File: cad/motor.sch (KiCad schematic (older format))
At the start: 12 parts, among them P2 CONN_2, P3 CONN_2, P4 CONN_2, Q1 SiA910EDJ, U5 DRV8837

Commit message: everything has a footprint
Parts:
- P2, P3, P4: footprint (none) -> Pin_Headers:Pin_Header_Straight_1x02
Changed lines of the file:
@@
 F 0 "P2" H 4400 2750 50  0000 C CNN
 F 1 "CONN_2" V 4500 2600 50  0000 C CNN
-F 2 "" H 4400 2600 60  0001 C CNN
+F 2 "Pin_Headers:Pin_Header_Straight_1x02" H 4400 2600 60  0001 C CNN
 F 3 "" H 4400 2600 60  0000 C CNN
 	1    4400 2600
@@
 F 0 "P3" H 7150 2750 50  0000 C CNN
 F 1 "CONN_2" V 7250 2600 50  0000 C CNN
-F 2 "" H 7150 2600 60  0001 C CNN
+F 2 "Pin_Headers:Pin_Header_Straight_1x02" H 7150 2600 60  0001 C CNN
 F 3 "" H 7150 2600 60  0000 C CNN
 	1    7150 2600
@@
 F 0 "P4" H 7500 5100 50  0000 C CNN
 F 1 "CONN_2" V 7600 4950 50  0000 C CNN
-F 2 "" H 7500 4950 60  0001 C CNN
+F 2 "Pin_Headers:Pin_Header_Straight_1x02" H 7500 4950 60  0001 C CNN
 F 3 "" H 7500 4950 60  0000 C CNN
 	1    7500 4950

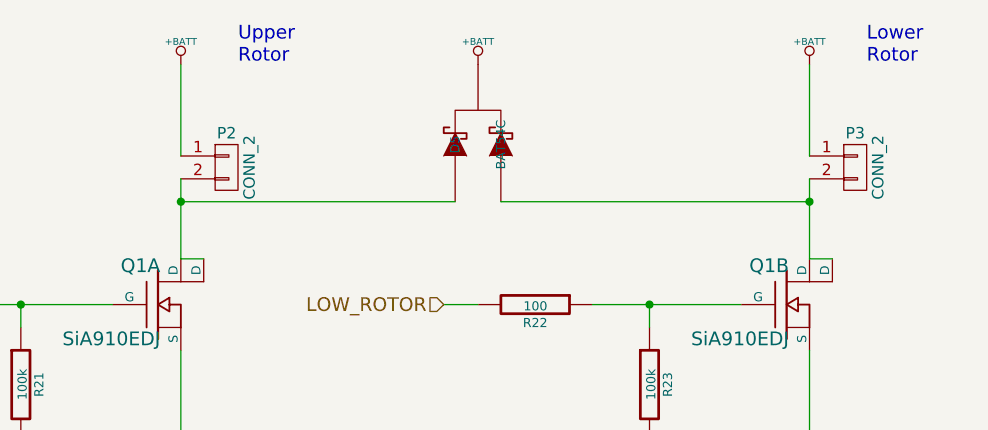
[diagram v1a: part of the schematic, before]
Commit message: made motor pads single to save space
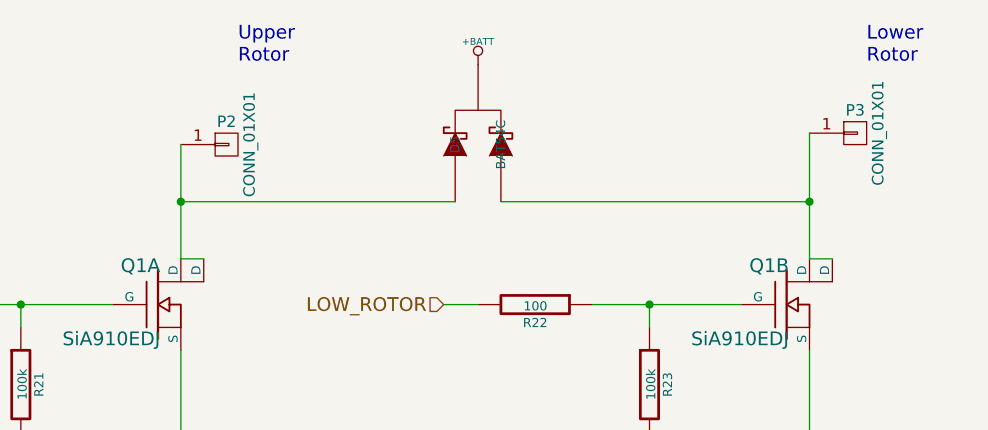
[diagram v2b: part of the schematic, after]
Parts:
- removed P2, P3: CONN_2, Pin_Headers:Pin_Header_Straight_1x02, symbol CONN_01X02
- added P2, P3: CONN_01X01, Pin_Headers:Pin_Header_Straight_1x01, symbol CONN_01X01
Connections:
- net at D5.1, Q1.6 (D), Q1.D1 (D): now also P2.1 (P1)
- net at D5.2, Q1.3 (D), Q1.D2 (D): now also P3.1 (P1)
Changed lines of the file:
@@
 Comment4 ""
 $EndDescr
-$Comp
-L CONN_01X02 P2
-U 1 1 54913051
-P 4400 2600
-F 0 "P2" H 4400 2750 50  0000 C CNN
-F 1 "CONN_2" V 4500 2600 50  0000 C CNN
-F 2 "Pin_Headers:Pin_Header_Straight_1x02" H 4400 2600 60  0001 C CNN
-F 3 "" H 4400 2600 60  0000 C CNN
-	1    4400 2600
-	1    0    0    -1
-$EndComp
-Wire Wire Line
-	4200 2650 4200 3000
-$Comp
-L +BATT #PWR070
-U 1 1 549132CE
-P 4200 2150
-F 0 "#PWR070" H 4200 2100 20  0001 C CNN
-F 1 "+BATT" H 4200 2250 30  0000 C CNN
-F 2 "" H 4200 2150 60  0000 C CNN
-F 3 "" H 4200 2150 60  0000 C CNN
-	1    4200 2150
-	1    0    0    -1
-$EndComp
-Wire Wire Line
-	4200 2150 4200 2550
+Wire Wire Line
+	4200 2500 4200 3000
 Connection ~ 4200 2750
 $Comp
@@
 	2600 3200 2750 3200
 $Comp
-L GND #PWR071
+L GND #PWR070
 U 1 1 54913D81
 P 4200 3900
-F 0 "#PWR071" H 4200 3900 30  0001 C CNN
+F 0 "#PWR070" H 4200 3900 30  0001 C CNN
 F 1 "GND" H 4200 3830 30  0001 C CNN
 F 2 "" H 4200 3900 60  0000 C CNN
@@
 $EndComp
 Connection ~ 4200 3800
-$Comp
-L CONN_01X02 P3
-U 1 1 54914313
-P 7150 2600
-F 0 "P3" H 7150 2750 50  0000 C CNN
-F 1 "CONN_2" V 7250 2600 50  0000 C CNN
-F 2 "Pin_Headers:Pin_Header_Straight_1x02" H 7150 2600 60  0001 C CNN
-F 3 "" H 7150 2600 60  0000 C CNN
-	1    7150 2600
-	1    0    0    -1
-$EndComp
-Wire Wire Line
-	6950 2650 6950 3000
-$Comp
-L +BATT #PWR072
-U 1 1 54914320
-P 6950 2150
-F 0 "#PWR072" H 6950 2100 20  0001 C CNN
-F 1 "+BATT" H 6950 2250 30  0000 C CNN
-F 2 "" H 6950 2150 60  0000 C CNN
-F 3 "" H 6950 2150 60  0000 C CNN
-	1    6950 2150
-	1    0    0    -1
-$EndComp
-Wire Wire Line
-	6950 2150 6950 2550
+Wire Wire Line
+	6950 2450 6950 3000
 Connection ~ 6950 2750
 $Comp
@@
 	5350 3200 5500 3200
 $Comp
-L GND #PWR073
+L GND #PWR071
 U 1 1 5491433E
 P 6950 3900
-F 0 "#PWR073" H 6950 3900 30  0001 C CNN
+F 0 "#PWR071" H 6950 3900 30  0001 C CNN
 F 1 "GND" H 6950 3830 30  0001 C CNN
 F 2 "" H 6950 3900 60  0000 C CNN
@@
 $EndComp
 $Comp
-L VCC #PWR074
+L VCC #PWR072
 U 1 1 5491AD60
 P 5550 5300
-F 0 "#PWR074" H 5550 5400 30  0001 C CNN
+F 0 "#PWR072" H 5550 5400 30  0001 C CNN
 F 1 "VCC" H 5550 5400 30  0000 C CNN
 F 2 "" H 5550 5300 60  0000 C CNN
@@
 $EndComp
 $Comp
-L DGND #PWR075
+L DGND #PWR073
 U 1 1 5491B7C8
 P 5550 5850
-F 0 "#PWR075" H 5550 5850 40  0001 C CNN
+F 0 "#PWR073" H 5550 5850 40  0001 C CNN
 F 1 "DGND" H 5550 5780 40  0000 C CNN
 F 2 "" H 5550 5850 60  0000 C CNN
@@
 Connection ~ 5550 5350
 $Comp
-L +BATT #PWR076
+L +BATT #PWR074
 U 1 1 5491B876
 P 5950 5550
-F 0 "#PWR076" H 5950 5500 20  0001 C CNN
+F 0 "#PWR074" H 5950 5500 20  0001 C CNN
 F 1 "+BATT" H 5950 5650 30  0000 C CNN
 F 2 "" H 5950 5550 60  0000 C CNN
@@
 $EndComp
 $Comp
-L GND #PWR077
+L GND #PWR075
 U 1 1 5491BB74
 P 5950 6100
-F 0 "#PWR077" H 5950 6100 30  0001 C CNN
+F 0 "#PWR075" H 5950 6100 30  0001 C CNN
 F 1 "GND" H 5950 6030 30  0001 C CNN
 F 2 "" H 5950 6100 60  0000 C CNN
@@
 	6100 5100 6200 5100
 $Comp
-L GND #PWR078
+L GND #PWR076
 U 1 1 5491EB14
 P 7250 5600
-F 0 "#PWR078" H 7250 5600 30  0001 C CNN
+F 0 "#PWR076" H 7250 5600 30  0001 C CNN
 F 1 "GND" H 7250 5530 30  0001 C CNN
 F 2 "" H 7250 5600 60  0000 C CNN
@@
 	6950 2750 5600 2750
 $Comp
-L +BATT #PWR079
+L +BATT #PWR077
 U 1 1 5493ADFB
 P 5500 2150
-F 0 "#PWR079" H 5500 2100 20  0001 C CNN
+F 0 "#PWR077" H 5500 2100 20  0001 C CNN
 F 1 "+BATT" H 5500 2250 30  0000 C CNN
 F 2 "" H 5500 2150 60  0000 C CNN
@@
 	1    0    0    -1
 $EndComp
+$Comp
+L CONN_01X01 P2
+U 1 1 549A1D34
+P 4400 2500
+F 0 "P2" H 4400 2600 50  0000 C CNN
+F 1 "CONN_01X01" V 4500 2500 50  0000 C CNN
+F 2 "Pin_Headers:Pin_Header_Straight_1x01" H 4400 2500 60  0001 C CNN
+F 3 "" H 4400 2500 60  0000 C CNN
+	1    4400 2500
+	1    0    0    -1
+$EndComp
+$Comp
+L CONN_01X01 P3
+U 1 1 549A2590
+P 7150 2450
+F 0 "P3" H 7150 2550 50  0000 C CNN
+F 1 "CONN_01X01" V 7250 2450 50  0000 C CNN
+F 2 "Pin_Headers:Pin_Header_Straight_1x01" H 7150 2450 60  0001 C CNN
+F 3 "" H 7150 2450 60  0000 C CNN
+	1    7150 2450
+	1    0    0    -1
+$EndComp

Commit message: routed some stuff
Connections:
- net at P2.1 (P1), Q1.6 (D), Q1.D1 (D): now also D5.2; no longer D5.1
- net at P3.1 (P1), Q1.3 (D), Q1.D2 (D): now also D5.1; no longer D5.2
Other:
- moved on the sheet: D5
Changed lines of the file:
@@
 Connection ~ 6950 3800
-$Comp
-L BAT54C D5
-U 1 1 54918821
-P 5500 2500
-F 0 "D5" H 5500 2600 40  0000 C CNN
-F 1 "BAT54C" H 5500 2400 40  0000 C CNN
-F 2 "Diodes_SMD:Diode_SOT23" H 5500 2500 60  0001 C CNN
-F 3 "" H 5500 2500 60  0000 C CNN
-F 4 "BAT54C" H 5500 2500 60  0001 C CNN "MPN"
-	1    5500 2500
-	0    -1   -1   0
-$EndComp
 $Comp
 L SiA910EDJ Q1
@@
 Text Notes 7100 4600 0    60   ~ 0
 Tail\nRotor
-Wire Wire Line
-	4200 2750 5400 2750
-Wire Wire Line
-	6950 2750 5600 2750
 $Comp
 L +BATT #PWR077
 U 1 1 5493ADFB
-P 5500 2150
-F 0 "#PWR077" H 5500 2100 20  0001 C CNN
-F 1 "+BATT" H 5500 2250 30  0000 C CNN
-F 2 "" H 5500 2150 60  0000 C CNN
-F 3 "" H 5500 2150 60  0000 C CNN
-	1    5500 2150
+P 5500 1950
+F 0 "#PWR077" H 5500 1900 20  0001 C CNN
+F 1 "+BATT" H 5500 2050 30  0000 C CNN
+F 2 "" H 5500 1950 60  0000 C CNN
+F 3 "" H 5500 1950 60  0000 C CNN
+	1    5500 1950
 	1    0    0    -1
 $EndComp
@@
 	1    0    0    -1
 $EndComp
+Wire Wire Line
+	5500 1950 5500 2000
+$Comp
+L BAT54C D5
+U 1 1 54918821
+P 5500 2350
+F 0 "D5" H 5500 2450 40  0000 C CNN
+F 1 "BAT54C" H 5500 2250 40  0000 C CNN
+F 2 "Diodes_SMD:Diode_SOT23" H 5500 2350 60  0001 C CNN
+F 3 "" H 5500 2350 60  0000 C CNN
+F 4 "BAT54C" H 5500 2350 60  0001 C CNN "MPN"
+	1    5500 2350
+	0    -1   -1   0
+$EndComp
+Wire Wire Line
+	6950 2750 5400 2750
+Wire Wire Line
+	5400 2750 5400 2600
+Wire Wire Line
+	4200 2750 5100 2750
+Wire Wire Line
+	5100 2750 5100 2650
+Wire Wire Line
+	5100 2650 5600 2650
+Wire Wire Line
+	5600 2650 5600 2600
 $EndSCHEMATC
